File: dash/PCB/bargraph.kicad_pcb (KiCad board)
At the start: 2 copper layers, 83 parts, among them IC1 ATMEGA328-P, U1 CH340G, U2 7805, X1 CRYSTAL_SMD, X2 CRYSTAL_SMD

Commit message: One of the boards completed at least
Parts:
- removed D16: LED, Diodes_SMD:MELF_Handsoldering
- added AFF1: LTS-6980HR, addlol:7seg, F.Cu at (105.7, 80.3)
- added D13: LED, LEDs:LED-5MM, F.Cu at (128.3, 31.8)
- added D14: LED, LEDs:LED-5MM, F.Cu at (109.2, 31.8)
- added D15: LED, LEDs:LED-5MM, F.Cu at (121.9, 31.8)
- added H1: pin_header_10, Pin_Headers:Pin_Header_Straight_1x10, F.Cu at (131.5, 105.5)
- added J1: DB9, Connect:DB9FC, B.Cu at (174.0, 123.9)
- added P1: USB_OTG, Connect:USB_Micro-B_10103594-0001LF, B.Cu at (67.3, 121.3)
- added P2: CONN_02X05, Pin_Headers:Pin_Header_Straight_2x05, F.Cu at (87.0, 81.3)
- added P3: CONN_02X05, Pin_Headers:Pin_Header_Straight_2x05, F.Cu at (87.0, 101.0)
- added P4: CONN_02X05, Pin_Headers:Pin_Header_Straight_2x05, F.Cu at (148.1, 80.7)
- added P5: CONN_02X05, Pin_Headers:Pin_Header_Straight_2x05, F.Cu at (148.0, 101.0)
- added Q1: BC557, TO_SOT_Packages_THT:TO-92_Inline_Wide, F.Cu at (207.0, 171.4)
- added Q2: BC547, TO_SOT_Packages_THT:TO-92_Inline_Wide, B.Cu at (217.0, 176.1)
- added U3: arduino_mini, addlol:arduino_nano, F.Cu at (119.4, 121.3)
- added U4: 74HC4094, Housings_DIP:DIP-16_W7.62mm, F.Cu at (81.5, 50.5)
- added U5: 74HC4094, Housings_DIP:DIP-16_W7.62mm, F.Cu at (94.7, 50.5)
- added U6: 74HC4094, Housings_DIP:DIP-16_W7.62mm, F.Cu at (155.9, 68.0)
- added U7: 74HC4094, Housings_DIP:DIP-16_W7.62mm, F.Cu at (141.0, 68.0)
- C4: value CP1 -> 470n
- C5: value CP1 -> 100u; footprint Capacitors_SMD:C_0805_HandSoldering -> Capacitors_SMD:c_elec_6.3x5.8
- D17: footprint Diodes_SMD:MELF_Handsoldering -> LEDs:LED-5MM
- D3: footprint Diodes_SMD:MELF_Handsoldering -> Diodes_SMD:SOD-123
- R13, R14, R15, R16, R17, R18, R19, R20, R21, R22, R23, R24, R25, R26, R27, R28, R29, R30, R31, R32, R33, R34, R35, R36, R37, R39, R41, R42, R43, R44, R46, R47, U1: moved to B.Cu
- R45: value 3k3 -> 2k7
- R48: value 100R -> 60R; moved to B.Cu
- X1, X2: footprint SMD_Packages:Ceramic_Filter -> addlol:cer_res
- moved D4 289.0 mm to (229.8, 158.3), turned to 90 degrees
- moved R40 266.9 mm to (210.3, 164.3), turned to 90 degrees
- moved R45 264.4 mm to (215.2, 153.6), turned to 270 degrees
- moved R38 263.1 mm to (205.1, 164.7), turned to 90 degrees
- moved X1 253.8 mm to (230.7, 124.7), turned to 90 degrees
- moved C6 253.3 mm to (226.1, 114.3), turned to 270 degrees
- moved R3 250.5 mm to (212.1, 133.3), turned to 270 degrees
- moved R9 249.8 mm to (232.4, 91.4), turned to 90 degrees
- moved U2 246.7 mm to (212.1, 82.5), turned to 270 degrees
- moved D2 242.7 mm to (217.2, 102.9), turned to 270 degrees
- moved C4 238.6 mm to (212.1, 114.3), turned to 270 degrees
- moved D3 229.7 mm to (212.1, 123.2), turned to 90 degrees
- moved C5 221.3 mm to (201.9, 85.1)
- moved X2 208.1 mm to (149.9, 148.0), turned to 90 degrees
- moved R6 205.9 mm to (157.5, 132.7), turned to 270 degrees
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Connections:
- net Net-(Q2-Pad1) renamed /intShiftLight
- C1 pad 1: /vcc -> /Vcc
- D5 pad 1: Net-(D5-Pad1) -> /D9
- D5 pad 2: Net-(D5-Pad2) -> GNDREF
- D6 pad 1: Net-(D6-Pad1) -> /D10
- D6 pad 2: Net-(D6-Pad2) -> GNDREF
- D7 pad 1: Net-(D7-Pad1) -> /D2
- D7 pad 2: Net-(D7-Pad2) -> GNDREF
- D8 pad 1: Net-(D8-Pad1) -> /D11
- D8 pad 2: Net-(D8-Pad2) -> GNDREF
- R13 pad 1: /U1_0 -> Net-(R13-Pad1)
- R13 pad 2: Net-(R13-Pad2) -> GNDREF
- R14 pad 1: /U1_1 -> Net-(R14-Pad1)
- R14 pad 2: Net-(R14-Pad2) -> GNDREF
- R15 pad 1: /U1_2 -> Net-(R15-Pad1)
- R15 pad 2: Net-(R15-Pad2) -> GNDREF
- R16 pad 1: /U1_3 -> Net-(R16-Pad1)
- R16 pad 2: Net-(R16-Pad2) -> GNDREF
- R17 pad 1: /U1_4 -> Net-(R17-Pad1)
- R17 pad 2: Net-(R17-Pad2) -> GNDREF
- R18 pad 1: /U1_5 -> Net-(R18-Pad1)
- R18 pad 2: Net-(R18-Pad2) -> GNDREF
- R19 pad 1: /U1_6 -> Net-(R19-Pad1)
- R19 pad 2: Net-(R19-Pad2) -> GNDREF
- R20 pad 1: /U1_7 -> Net-(R20-Pad1)
- R20 pad 2: Net-(R20-Pad2) -> GNDREF
- R21 pad 1: /U2_0 -> Net-(R21-Pad1)
- R21 pad 2: Net-(R21-Pad2) -> GNDREF
- R22 pad 1: /U2_1 -> Net-(R22-Pad1)
- R22 pad 2: Net-(R22-Pad2) -> GNDREF
- R23 pad 1: /U2_2 -> Net-(R23-Pad1)
- R23 pad 2: Net-(R23-Pad2) -> GNDREF
- R24 pad 1: /U2_3 -> Net-(R24-Pad1)
- R24 pad 2: Net-(R24-Pad2) -> GNDREF
- R25 pad 1: /U2_4 -> Net-(R25-Pad1)
- R25 pad 2: Net-(R25-Pad2) -> GNDREF
- R26 pad 1: /U2_5 -> Net-(R26-Pad1)
- R26 pad 2: Net-(R26-Pad2) -> GNDREF
- R27 pad 1: /U2_6 -> Net-(R27-Pad1)
- R27 pad 2: Net-(R27-Pad2) -> GNDREF
- R28 pad 1: /U2_7 -> Net-(R28-Pad1)
- R28 pad 2: Net-(R28-Pad2) -> GNDREF
- R29 pad 1: /U3_0 -> Net-(R29-Pad1)
- R29 pad 2: Net-(R29-Pad2) -> GNDREF
- R30 pad 1: /U3_1 -> Net-(R30-Pad1)
- R30 pad 2: Net-(R30-Pad2) -> GNDREF
- R31 pad 1: /U3_2 -> Net-(R31-Pad1)
- R31 pad 2: Net-(R31-Pad2) -> GNDREF
- R32 pad 1: /U3_3 -> Net-(R32-Pad1)
- R32 pad 2: Net-(R32-Pad2) -> GNDREF
- R33 pad 1: /U3_4 -> Net-(R33-Pad1)
- R33 pad 2: Net-(R33-Pad2) -> GNDREF
- R34 pad 1: /U3_5 -> Net-(R34-Pad1)
- R34 pad 2: Net-(R34-Pad2) -> GNDREF
- R35 pad 1: /U3_6 -> Net-(R35-Pad1)
- R35 pad 2: Net-(R35-Pad2) -> GNDREF
- R36 pad 1: /U3_7 -> Net-(R36-Pad1)
- R36 pad 2: Net-(R36-Pad2) -> GNDREF
- U1 pad 1: GNDREF -> /Vcc
- U1 pad 13: /DTR -> Net-(C6-Pad1)
- U1 pad 14: Net-(U1-Pad14) -> /tx
- U1 pad 15: /vcc -> /rx
- U1 pad 16: /vcc -> GNDREF
- U1 pad 4: Net-(C6-Pad1) -> /DTR
- X1 pad 1: Net-(U1-Pad8) -> Net-(U1-Pad9)
- X1 pad 2: Net-(U1-Pad7) -> Net-(U1-Pad10)
- bar_green1 pad 1: Net-(R13-Pad2) -> /U1_0
- bar_green1 pad 10: Net-(R22-Pad2) -> /U2_1
- bar_green1 pad 11: GNDREF -> Net-(R22-Pad1)
- bar_green1 pad 12: GNDREF -> Net-(R21-Pad1)
- bar_green1 pad 13: GNDREF -> Net-(R20-Pad1)
- bar_green1 pad 14: GNDREF -> Net-(R19-Pad1)
- bar_green1 pad 15: GNDREF -> Net-(R18-Pad1)
- bar_green1 pad 16: GNDREF -> Net-(R17-Pad1)
- bar_green1 pad 17: GNDREF -> Net-(R16-Pad1)
- bar_green1 pad 18: GNDREF -> Net-(R15-Pad1)
- bar_green1 pad 19: GNDREF -> Net-(R14-Pad1)
- bar_green1 pad 2: Net-(R14-Pad2) -> /U1_1
- bar_green1 pad 20: GNDREF -> Net-(R13-Pad1)
- bar_green1 pad 3: Net-(R15-Pad2) -> /U1_2
- bar_green1 pad 4: Net-(R16-Pad2) -> /U1_3
- bar_green1 pad 5: Net-(R17-Pad2) -> /U1_4
- bar_green1 pad 6: Net-(R18-Pad2) -> /U1_5
- bar_green1 pad 7: Net-(R19-Pad2) -> /U1_6
- bar_green1 pad 8: Net-(R20-Pad2) -> /U1_7
- bar_green1 pad 9: Net-(R21-Pad2) -> /U2_0
- bar_red1 pad 1: Net-(R33-Pad2) -> /U3_4
- bar_red1 pad 11: GNDREF -> Net-(bar_red1-Pad11)
- bar_red1 pad 12: GNDREF -> Net-(bar_red1-Pad12)
- bar_red1 pad 13: GNDREF -> Net-(bar_red1-Pad13)
- bar_red1 pad 14: GNDREF -> Net-(bar_red1-Pad14)
- bar_red1 pad 15: GNDREF -> Net-(bar_red1-Pad15)
- bar_red1 pad 16: GNDREF -> Net-(bar_red1-Pad16)
- bar_red1 pad 17: GNDREF -> Net-(R36-Pad1)
- bar_red1 pad 18: GNDREF -> Net-(R35-Pad1)
- bar_red1 pad 19: GNDREF -> Net-(R34-Pad1)
- bar_red1 pad 2: Net-(R34-Pad2) -> /U3_5
- bar_red1 pad 20: GNDREF -> Net-(R33-Pad1)
- bar_red1 pad 3: Net-(R35-Pad2) -> /U3_6
- bar_red1 pad 4: Net-(R36-Pad2) -> /U3_7
- bar_ylw1 pad 1: Net-(R23-Pad2) -> /U2_2
- bar_ylw1 pad 10: Net-(R32-Pad2) -> /U3_3
- bar_ylw1 pad 11: GNDREF -> Net-(R32-Pad1)
- bar_ylw1 pad 12: GNDREF -> Net-(R31-Pad1)
- bar_ylw1 pad 13: GNDREF -> Net-(R30-Pad1)
- bar_ylw1 pad 14: GNDREF -> Net-(R29-Pad1)
- bar_ylw1 pad 15: GNDREF -> Net-(R28-Pad1)
- bar_ylw1 pad 16: GNDREF -> Net-(R27-Pad1)
- bar_ylw1 pad 17: GNDREF -> Net-(R26-Pad1)
- bar_ylw1 pad 18: GNDREF -> Net-(R25-Pad1)
- bar_ylw1 pad 19: GNDREF -> Net-(R24-Pad1)
- bar_ylw1 pad 2: Net-(R24-Pad2) -> /U2_3
- bar_ylw1 pad 20: GNDREF -> Net-(R23-Pad1)
- bar_ylw1 pad 3: Net-(R25-Pad2) -> /U2_4
- bar_ylw1 pad 4: Net-(R26-Pad2) -> /U2_5
- bar_ylw1 pad 5: Net-(R27-Pad2) -> /U2_6
- bar_ylw1 pad 6: Net-(R28-Pad2) -> /U2_7
- bar_ylw1 pad 7: Net-(R29-Pad2) -> /U3_0
- bar_ylw1 pad 8: Net-(R30-Pad2) -> /U3_1
- bar_ylw1 pad 9: Net-(R31-Pad2) -> /U3_2
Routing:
- net GNDREF: track 0.00 -> 297.0 mm, vias 0 -> 4
- net /D5: track 0.00 -> 147.2 mm, vias 0 -> 4
- net /intShiftLight: track 0.00 -> 129.1 mm
- net /Vcc: track 0.00 -> 106.5 mm
- net /12vraw: track 0.00 -> 105.5 mm
- net Net-(R42-Pad2): track 0.00 -> 70.2 mm
- net /D6: track 0.00 -> 68.3 mm, vias 0 -> 1
- net /D7: track 0.00 -> 66.6 mm
- net Net-(U5-Pad9): track 0.00 -> 61.9 mm, vias 0 -> 3
- net /D8: track 0.00 -> 57.0 mm, vias 0 -> 1
- net Net-(R41-Pad2): track 0.00 -> 44.4 mm
- net /U3_0: track 0.00 -> 44.1 mm, vias 0 -> 1
- net /U3_1: track 0.00 -> 40.8 mm, vias 0 -> 1
- net /U3_2: track 0.00 -> 35.4 mm, vias 0 -> 1
- net Net-(R44-Pad2): track 0.00 -> 32.9 mm
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- added copper zone on B.Cu, net GNDREF
- added copper zone on F.Cu, net GNDREF
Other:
- board outline added: 100 x 59.1 mm
- net class Default: via_dia 0.6 -> 1.5; via_drill 0.4 -> 0.8
- net class extra width added: clearance 0.2, trace_width 0.5, via_dia 2, via_drill 0.8
- rule via_min_drill: 0.3 -> 0.8
- rule via_min_size: 0.4 -> 1.2
- board text added: "Arnþór Gíslason 2016"
- board text added: "HVR-2 2016"

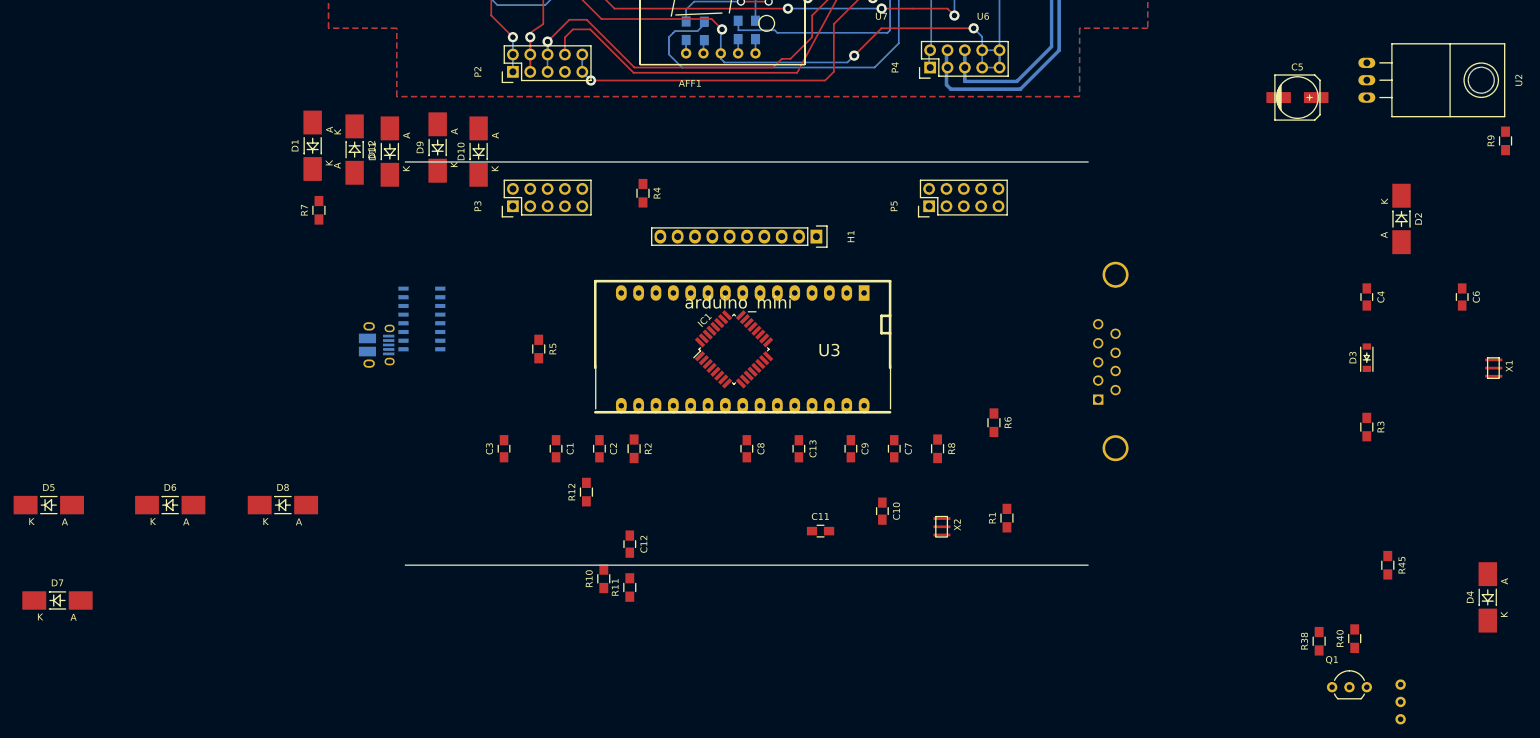
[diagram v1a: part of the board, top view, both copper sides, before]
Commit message: Fixing bugs in the PCB designe
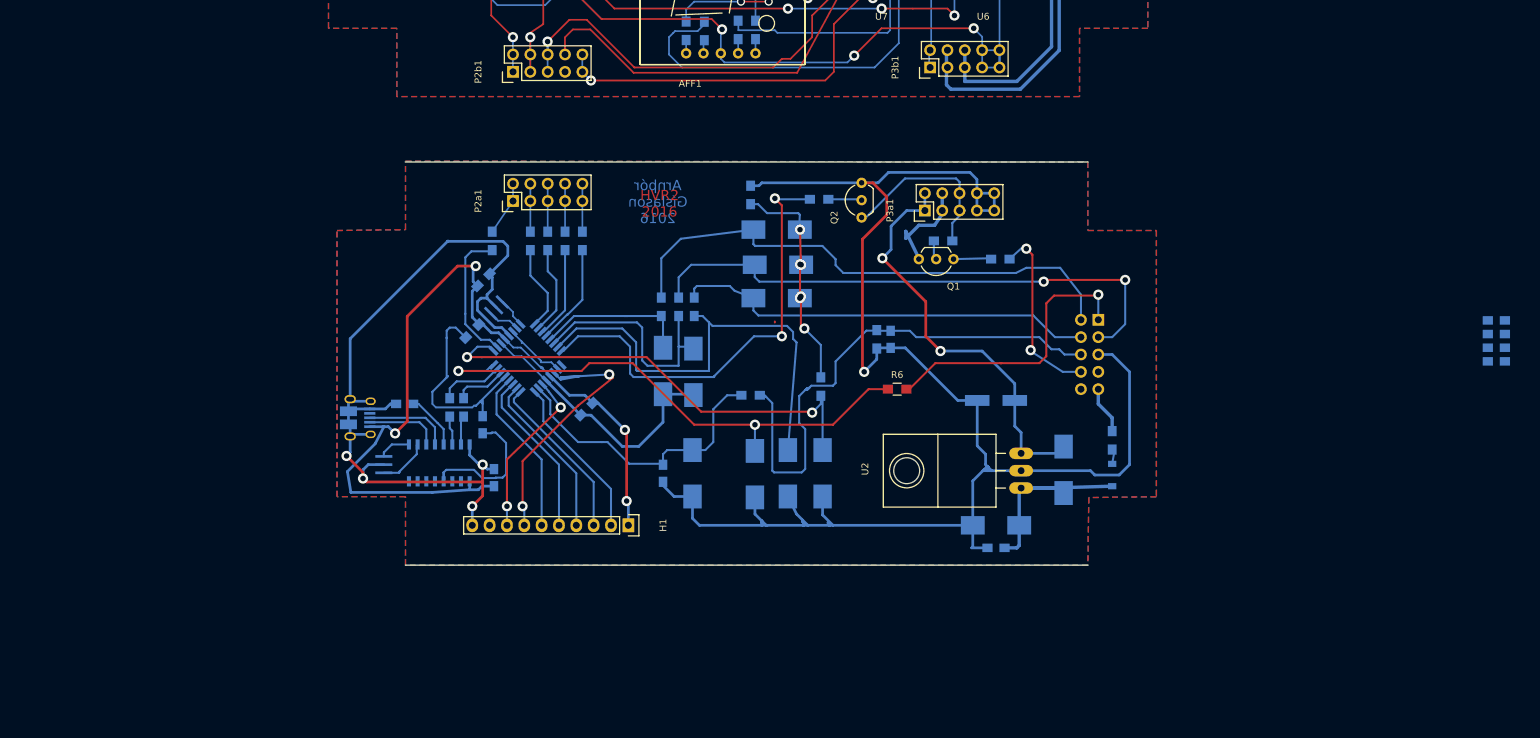
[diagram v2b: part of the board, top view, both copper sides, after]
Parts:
- removed P2, P3, P4, P5: CONN_02X05, Pin_Headers:Pin_Header_Straight_2x05
- removed U3: arduino_mini, addlol:arduino_nano
- added P2a1: CONN_02X05, Pin_Headers:Pin_Header_Straight_2x05, F.Cu at (87.0, 100.2)
- added P2b1: CONN_02X05, Pin_Headers:Pin_Header_Straight_2x05, F.Cu at (87.0, 81.3)
- added P3a1: CONN_02X05, Pin_Headers:Pin_Header_Straight_2x05, F.Cu at (147.4, 101.6)
- added P3b1: CONN_02X05, Pin_Headers:Pin_Header_Straight_2x05, F.Cu at (148.1, 80.7)
- added R49: 1k, Resistors_SMD:R_0805_HandSoldering, B.Cu at (94.7, 106.1)
- added R50: 1kR, Resistors_SMD:R_0805_HandSoldering, B.Cu at (97.2, 106.1)
- added R51: R, Resistors_SMD:R_0805_HandSoldering, B.Cu at (84.0, 106.1)
- added R52: 1k, Resistors_SMD:R_0805_HandSoldering, B.Cu at (89.6, 106.1)
- added R53: 1k, Resistors_SMD:R_0805_HandSoldering, B.Cu at (92.1, 106.1)
- AFF1: value LTS-6980HR -> 7SEGMENTS
- C1, C10, C11, C12, C13, C2, C3, C4, C5, C6, C7, C8, C9, D1, D10, D11, D12, D2, D3, D4, D5, D6, D7, D8, D9, IC1, R1, R10, R11, R12, R2, R3, R38, R4, R40, R45, R5, R7, R8, R9, X1, X2: moved to B.Cu
- J1: footprint Connect:DB9FC -> Pin_Headers:Pin_Header_Straight_2x05
- Q2: moved to F.Cu
- U2: value 7805 -> LM7805CT; footprint TO_SOT_Packages_THT:TO-220_Neutral123_Horizontal -> TO_SOT_Packages_THT:TO-220_Neutral123_Horizontal_LargePads
- moved X1 163.2 mm to (68.1, 138.9), turned to 270 degrees
- moved R9 157.5 mm to (79.8, 130.5)
- moved C6 155.7 mm to (71.2, 130.0), turned to 180 degrees
- moved C1 138.5 mm to (231.1, 121.7), turned to 0 degrees
- moved C12 129.7 mm to (231.1, 123.7), turned to 0 degrees
- moved D1 119.8 mm to (167.7, 139.6)
- moved C8 111.1 mm to (231.1, 119.7), turned to 0 degrees
- moved D2 110.3 mm to (113.3, 140.1)
- moved Q2 107.9 mm to (138.1, 102.7)
- moved C13 103.9 mm to (231.1, 117.7), turned to 0 degrees
- moved D7 103.8 mm to (122.5, 140.2), turned to 270 degrees
- moved R45 99.1 mm to (131.9, 100.0), turned to 180 degrees
- moved D5 92.1 mm to (109.0, 125.1), turned to 270 degrees
- moved R40 83.8 mm to (150.0, 106.1), turned to 0 degrees
- moved Q1 83.7 mm to (151.6, 108.8), turned to 180 degrees
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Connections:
- AFF1 pad 3: GNDREF -> /Vcc
- AFF1 pad 8: GNDREF -> /Vcc
- H1 pad 9: /D12 -> Net-(H1-Pad9)
- J1 pad 6: /12Vraw -> /oilP
- J1 pad 7: /oilP -> Net-(J1-Pad7)
- J1 pad 9: Net-(J1-Pad9) -> /12Vraw
- U2 pad 1: GNDREF -> Net-(C4-Pad1)
- U2 pad 2: /Vcc -> GNDREF
- U2 pad 3: Net-(C4-Pad1) -> /Vcc
- X1 pad 2: Net-(U1-Pad10) -> GNDREF
- X1 pad 3: GNDREF -> Net-(U1-Pad10)
- X2 pad 1: Net-(IC1-Pad8) -> Net-(IC1-Pad7)
- X2 pad 2: Net-(IC1-Pad7) -> GNDREF
- X2 pad 3: GNDREF -> Net-(IC1-Pad8)
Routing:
- net /Vcc: track 106.5 -> 444.9 mm, vias 0 -> 9
- net GNDREF: track 297.0 -> 550.4 mm, vias 4 -> 6
- net /gearDown: track 0.00 -> 82.5 mm, vias 0 -> 2
- net /gearUp: track 0.00 -> 78.7 mm
- net /D2: track 0.00 -> 78.6 mm, vias 0 -> 2
- net /oilP: track 0.00 -> 78.3 mm
- net /D3: track 0.00 -> 69.8 mm, vias 0 -> 2
- net /D11: track 0.00 -> 68.5 mm
- net /D12: track 0.00 -> 66.2 mm, vias 0 -> 2
- net /neutral: track 0.00 -> 62.0 mm
- net /A0: track 0.00 -> 43.7 mm
- net /A6: track 0.00 -> 42.4 mm, vias 0 -> 2
- net /rpm: track 0.00 -> 42.0 mm, vias 0 -> 1
- net /D10: track 0.00 -> 34.6 mm
- net Net-(D10-Pad1): track 0.00 -> 34.3 mm, vias 0 -> 6
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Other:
- net class 0.3 added: clearance 0.2, trace_width 0.3, via_dia 1.5, via_drill 0.8
- net class 0.4 added: clearance 0.2, trace_width 0.4, via_dia 1.5, via_drill 0.8
- net class 0.5 added: clearance 0.2, trace_width 0.5, via_dia 1.5, via_drill 0.8
- net class Default: trace_width 0.25 -> 0.3
- net class extra width removed
- board text added: "."
- board text added: "HVR2 2016"

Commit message: adding stuff
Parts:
- removed C12, C8: 100n, Capacitors_SMD:C_0805_HandSoldering
- removed P2a1, P2b1, P3a1, P3b1: CONN_02X05, Pin_Headers:Pin_Header_Straight_2x05
- added P2: CONN_01X05, Socket_Strips:Socket_Strip_Straight_1x05, B.Cu at (85.1, 98.5)
- added P3: CONN_01X05, Pin_Headers:Pin_Header_Straight_1x05, B.Cu at (85.1, 80.6)
- added P4: CONN_01X05, Socket_Strips:Socket_Strip_Straight_1x05, B.Cu at (144.8, 98.4)
- added P5: CONN_01X05, Pin_Headers:Pin_Header_Straight_1x05, B.Cu at (144.8, 80.6)
- added P6: CONN_01X02, Socket_Strips:Socket_Strip_Straight_1x02, F.Cu at (169.5, 107.9)
- C1, J1, R38, R45: moved to F.Cu
- C6: value C -> 100n
- Q1, Q2: moved to B.Cu
- R13, R14, R15, R16, R17, R18, R19, R20, R21, R22, R23, R24, R25, R26, R27, R28, R29, R30, R31, R32, R33, R34, R35, R36, R37, R39, R41, R42, R43, R44, R46, R47: value 560 -> 330
- moved C1 167.3 mm to (77.0, 56.6), turned to 270 degrees
- moved C13 93.3 mm to (159.9, 57.3), turned to 90 degrees
- moved X1 14.4 mm to (82.2, 135.8)
- moved R14 9.99 mm to (92.5, 39.4)
- moved R16 9.99 mm to (97.5, 39.4)
- moved R18 9.99 mm to (102.6, 39.4)
- moved R19 9.99 mm to (105.2, 39.4)
- moved R21 9.99 mm to (110.2, 39.4)
- moved R13 9.99 mm to (89.9, 39.4)
- moved R15 9.99 mm to (95.0, 39.4)
- moved R17 9.99 mm to (100.1, 39.4)
- moved R20 9.99 mm to (107.7, 39.4)
- moved R22 9.99 mm to (112.8, 39.4)
- moved bar_green1 9.91 mm to (89.8, 43.1)
- moved R8 9.38 mm to (73.8, 125.3), turned to 315 degrees
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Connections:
- AFF1 pad 3: /Vcc -> Net-(AFF1-Pad3)
- D13 pad 2: /12vraw -> /12vF
- D3 pad 2: Net-(D3-Pad2) -> /12vF
- H1 pad 7: /A6 -> Net-(H1-Pad7)
- IC1 pad 19: /A6 -> Net-(IC1-Pad19)
- J1 pad 2: /gearUp -> /gearDown
- J1 pad 3: /gearDown -> /neutral
- J1 pad 4: /neutral -> /gearUp
- J1 pad 5: GNDREF -> Net-(J1-Pad5)
- J1 pad 6: /oilP -> Net-(J1-Pad6)
- J1 pad 7: Net-(J1-Pad7) -> GNDREF
- J1 pad 8: /extShiftLight -> GNDREF
- J1 pad 9: /12Vraw -> /12vraw
- Q1 pad 3: /12vraw -> /12vF
- R3 pad 1: Net-(D3-Pad2) -> /12vF
- R3 pad 2: /12Vraw -> /12vraw
- U1 pad 1: /Vcc -> GNDREF
- U1 pad 11: Net-(P1-Pad2) -> Net-(U1-Pad11)
- U1 pad 12: Net-(P1-Pad3) -> Net-(U1-Pad12)
- U1 pad 13: Net-(C6-Pad1) -> /DTR
- U1 pad 14: /tx -> Net-(U1-Pad14)
- U1 pad 15: /rx -> Net-(U1-Pad15)
- U1 pad 16: GNDREF -> /Vcc
- U1 pad 4: /DTR -> Net-(C6-Pad1)
- U1 pad 5: Net-(U1-Pad5) -> Net-(P1-Pad3)
- U1 pad 6: Net-(U1-Pad6) -> Net-(P1-Pad2)
- X1 pad 1: Net-(U1-Pad9) -> Net-(U1-Pad8)
- X1 pad 3: Net-(U1-Pad10) -> Net-(U1-Pad7)
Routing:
- net GNDREF: track 550.4 -> 744.7 mm, vias 6 -> 7
- net /12vF: track 0.00 -> 160.5 mm, vias 0 -> 2
- net /12vraw: track 121.0 -> 9.34 mm, vias 0 -> 1
- net /A6: track 42.4 -> 0.00 mm, vias 2 -> 0
- net /oilP: track 78.3 -> 47.8 mm
- net /U2_1: track 21.2 -> 38.8 mm
- net /U2_5: track 23.6 -> 40.3 mm
- net /extShiftLight: track 27.2 -> 11.3 mm, vias 2 -> 0
- net (no net): track 0.13 -> 15.8 mm, vias 0 -> 6
- net /intShiftLight: track 156.1 -> 140.9 mm, vias 0 -> 2
- net /U2_0: track 18.2 -> 31.9 mm
- net /RST: track 32.6 -> 19.4 mm
- net /U2_4: track 20.9 -> 33.9 mm
- net /U1_7: track 22.4 -> 34.1 mm
- net /U1_6: track 18.8 -> 29.5 mm
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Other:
- board size 100 x 59.1 mm -> 120 x 127 mm
- board text added: "+"
- board text added: "D4 D5 D6 D7 D8"
- board text added: "Gnd NC A7 NC A5 A4 A3 A2 A1 Vcc"
- board text added: "Vcc 12V Shft Gnd Gnd"
- board text added: "gearD gearU NC Gnd NC"
- board text added: "rpm neut NC Gnd 12V"
- board text added: "v0.2"
- board text added: "|"

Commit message: committing very old unsaved changes
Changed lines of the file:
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@@
     (area 59.899999 25.899999 180.100001 153.100001)
     (thickness 1.6)
-    (drawings 46)
+    (drawings 45)
     (tracks 1447)
     (zones 0)
@@
     (40 Dwgs.User user)
     (41 Cmts.User user)
-    (42 Eco1.User user hide)
-    (43 Eco2.User user hide)
+    (42 Eco1.User user)
+    (43 Eco2.User user)
     (44 Edge.Cuts user)
     (45 Margin user)
@@
     (aux_axis_origin 174.9844 79.99348)
     (grid_origin 161.74364 116.12148)
-    (visible_elements 7FFFFF9F)
+    (visible_elements 7FFFFFFF)
     (pcbplotparams
-      (layerselection 0x00000_ffffffff)
+      (layerselection 0x01020_7ffffffe)
       (usegerberextensions false)
-      (excludeedgelayer true)
+      (excludeedgelayer false)
       (linewidth 0.100000)
       (plotframeref false)
@@
       (psnegative false)
       (psa4output false)
-      (plotreference true)
-      (plotvalue true)
+      (plotreference false)
+      (plotvalue false)
       (plotinvisibletext false)
       (padsonsilk false)
       (subtractmaskfromsilk false)
-      (outputformat 4)
-      (mirror true)
+      (outputformat 3)
+      (mirror false)
       (drillshape 2)
       (scaleselection 1)
-      (outputdirectory svg))
+      (outputdirectory dxf))
   )
   (net 0 "")
@@
   (target plus (at 174.99226 31.01468) (size 5) (width 0.2) (layer Edge.Cuts))
   (target plus (at 64.99226 31.01468) (size 5) (width 0.2) (layer Edge.Cuts))
-  (gr_line (start 60 85) (end 180 85) (angle 90) (layer Edge.Cuts) (width 0.2))
   (gr_text "HVR2 \n2016\n" (at 107.232 100.62444) (layer F.Cu)
     (effects (font (size 1.5 1.5) (thickness 0.3)))
